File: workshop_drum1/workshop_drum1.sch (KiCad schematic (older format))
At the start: 40 parts, among them J1 9v_Battery_Clip, J2 Trigger_Input, J3 Output, U1 LM358, U2 7414, U3 78L05

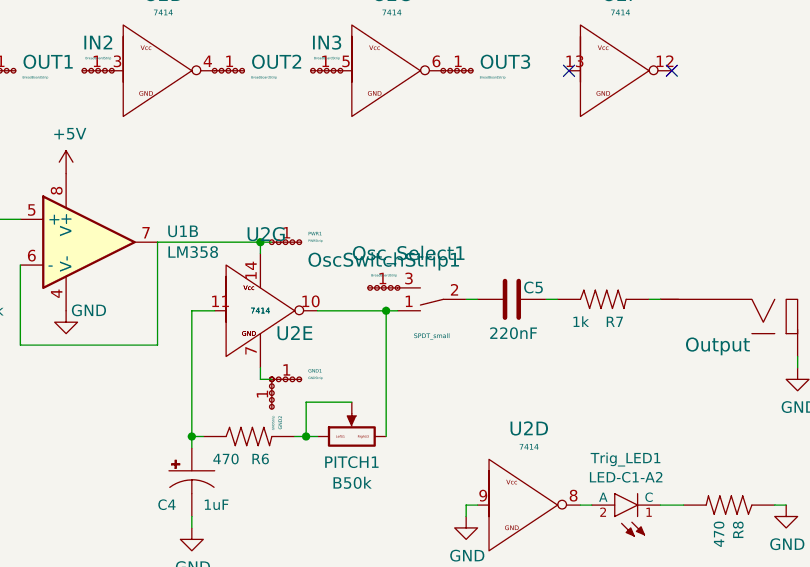
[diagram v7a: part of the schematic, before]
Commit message: got rid of square pins - printed gerbers - changed names- relayed traces
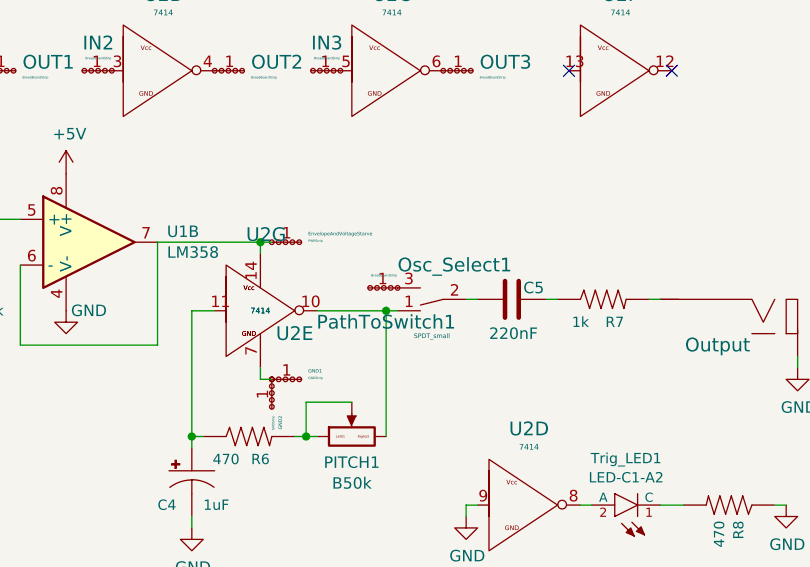
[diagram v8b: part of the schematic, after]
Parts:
- EnvelopeAndVoltageStarve: renamed from PWR1; footprint zfoot:GNDStrip -> zfoot:BreadBoardStrip_4
- GND1: footprint zfoot:GNDStrip -> zfoot:BreadBoardStripBold_4
- GND2: footprint zfoot:GNDStripLONG -> zfoot:BreadBoardStripBold_7
- IN1, IN2, IN3, OUT1, OUT2, OUT3: footprint zfoot:BreadBoardStrip -> zfoot:BreadBoardStrip_4
- PathToSwitch1: renamed from OscSwitchStrip1; footprint zfoot:BreadBoardStrip -> zfoot:BreadBoardStrip_4
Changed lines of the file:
@@
-EESchema Schematic File Version 3
+EESchema Schematic File Version 2
 LIBS:4ms-headers
 LIBS:4ms-ic
@@
 F 0 "IN1" H 3359 779 60  0000 C CNN
 F 1 "BreadBoardStrip" H 3359 845 10  0000 C CNN
-F 2 "zfoot:BreadBoardStrip" H 3170 880 60  0001 C CNN
+F 2 "zfoot:BreadBoardStrip_4" H 3170 880 60  0001 C CNN
 F 3 "" H 3300 900 60  0001 C CNN
 	1    3300 900
@@
 F 0 "OUT1" H 3909 937 60  0000 L CNN
 F 1 "BreadBoardStrip" H 3909 871 10  0000 L CNN
-F 2 "zfoot:BreadBoardStrip" H 3620 880 60  0001 C CNN
+F 2 "zfoot:BreadBoardStrip_4" H 3620 880 60  0001 C CNN
 F 3 "" H 3750 900 60  0001 C CNN
 	1    3750 900
@@
 F 0 "OUT3" H 5909 937 60  0000 L CNN
 F 1 "BreadBoardStrip" H 5909 871 10  0000 L CNN
-F 2 "zfoot:BreadBoardStrip" H 5620 880 60  0001 C CNN
+F 2 "zfoot:BreadBoardStrip_4" H 5620 880 60  0001 C CNN
 F 3 "" H 5750 900 60  0001 C CNN
 	1    5750 900
@@
 F 0 "OUT2" H 4909 937 60  0000 L CNN
 F 1 "BreadBoardStrip" H 4909 871 10  0000 L CNN
-F 2 "zfoot:BreadBoardStrip" H 4620 880 60  0001 C CNN
+F 2 "zfoot:BreadBoardStrip_4" H 4620 880 60  0001 C CNN
 F 3 "" H 4750 900 60  0001 C CNN
 	1    4750 900
@@
 F 0 "IN2" H 4359 779 60  0000 C CNN
 F 1 "BreadBoardStrip" H 4359 845 10  0000 C CNN
-F 2 "zfoot:BreadBoardStrip" H 4170 880 60  0001 C CNN
+F 2 "zfoot:BreadBoardStrip_4" H 4170 880 60  0001 C CNN
 F 3 "" H 4300 900 60  0001 C CNN
 	1    4300 900
@@
 F 0 "IN3" H 5359 779 60  0000 C CNN
 F 1 "BreadBoardStrip" H 5359 845 10  0000 C CNN
-F 2 "zfoot:BreadBoardStrip" H 5170 880 60  0001 C CNN
+F 2 "zfoot:BreadBoardStrip_4" H 5170 880 60  0001 C CNN
 F 3 "" H 5300 900 60  0001 C CNN
 	1    5300 900
@@
 F 0 "GND1" H 5159 2287 15  0000 L CNN
 F 1 "GNDStrip" H 5159 2256 10  0000 L CNN
-F 2 "zfoot:GNDStrip" H 4870 2230 60  0001 C CNN
+F 2 "zfoot:BreadBoardStripBold_4" H 4870 2230 60  0001 C CNN
 F 3 "" H 5000 2250 60  0001 C CNN
 	1    5000 2250
@@
 U 1 1 5A3358B6
 P 5700 1900
-F 0 "Osc_Select1" H 5800 1700 60  0000 C CNN
+F 0 "Osc_Select1" H 5600 1750 60  0000 C CNN
 F 1 "SPDT_small" H 5700 2060 20  0000 C CNN
 F 2 "zfoot:SPDT_Wired" H 5700 1900 60  0001 C CNN
@@
 	7200 2800 7250 2800
 $Comp
-L BreadBoardStrip OscSwitchStrip1
+L BreadBoardStrip PathToSwitch1
 U 1 1 5A33DD61
 P 5550 1850
-F 0 "OscSwitchStrip1" H 5609 1729 60  0000 C CNN
+F 0 "PathToSwitch1" H 5600 2000 60  0000 C CNN
 F 1 "BreadBoardStrip" H 5609 1795 10  0000 C CNN
-F 2 "zfoot:BreadBoardStrip" H 5420 1830 60  0001 C CNN
+F 2 "zfoot:BreadBoardStrip_4" H 5420 1830 60  0001 C CNN
 F 3 "" H 5550 1850 60  0001 C CNN
 	1    5550 1850
@@
 $EndComp
 $Comp
-L GNDStrip PWR1
+L GNDStrip EnvelopeAndVoltageStarve
 U 1 1 5A330F13
 P 5000 1650
-F 0 "PWR1" H 5159 1687 15  0000 L CNN
+F 0 "EnvelopeAndVoltageStarve" H 5159 1687 15  0000 L CNN
 F 1 "PWRStrip" H 5159 1656 10  0000 L CNN
-F 2 "zfoot:GNDStrip" H 4870 1630 60  0001 C CNN
+F 2 "zfoot:BreadBoardStrip_4" H 4870 1630 60  0001 C CNN
 F 3 "" H 5000 1650 60  0001 C CNN
 	1    5000 1650
@@
 F 0 "GND2" H 5159 2287 15  0000 L CNN
 F 1 "GNDStrip" H 5159 2256 10  0000 L CNN
-F 2 "zfoot:GNDStripLONG" H 4870 2230 60  0001 C CNN
+F 2 "zfoot:BreadBoardStripBold_7" H 4870 2230 60  0001 C CNN
 F 3 "" H 5000 2250 60  0001 C CNN
 	1    5000 2250
